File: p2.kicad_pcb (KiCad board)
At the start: 2 copper layers, 66 x 57 mm, 33 parts, among them J1 BARREL_JACK, J2 FLASH_JMP, J3 UART, J4 ALT_POWER, J5 jack-3.5mm-5pin, J6 jack-3.5mm-5pin, J7 jack-3.5mm-5pin, J8 jack-3.5mm-5pin, Q1 IRL540N, Q2 IRL540N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

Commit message: update to pcb-rev1.1
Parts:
- removed the REF** at (31.0, 23.5)
- removed the REF** at (31.0, 73.5)
- removed the REF*** at (47.0, 40.0)
- added REF**: Symbol_CreativeCommons_CopperTop_Type2_Small, Symbols:Symbol_CreativeCommons_CopperTop_Type2_Small, F.Cu at (34.0, 40.5)
- added REF**: Symbol_CC-ShareAlike_CopperTop_Small, Symbols:Symbol_CC-ShareAlike_CopperTop_Small, F.Cu at (45.0, 40.5)
- added REF**: Symbol_CC-Attribution_CopperTop_Small, Symbols:Symbol_CC-Attribution_CopperTop_Small, F.Cu at (39.5, 40.5)
- added REF***: OSHW-Logo2_9.8x8mm_SilkScreen, Symbols:OSHW-Logo2_9.8x8mm_SilkScreen, B.Cu at (58.5, 35.0)
- moved REF** 9.50 mm to (72.0, 36.0)
- moved G*** 1.29 mm to (72.5, 35.0)
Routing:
- net /12V: track 138.4 -> 133.4 mm
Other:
- outline, holes or cut-outs redrawn
- board text added: "+12V"
- board text added: "GND"
- board text added: "Short to flash"
- board text added: "WaterControl v2 r1.1"
- board text added: "designed with"
- board text added: "https://github.com/mqus/watercontrol-pcb.git"
- board text removed: "Flash"
- board text removed: "GND+12V"
- board text removed: "made with"

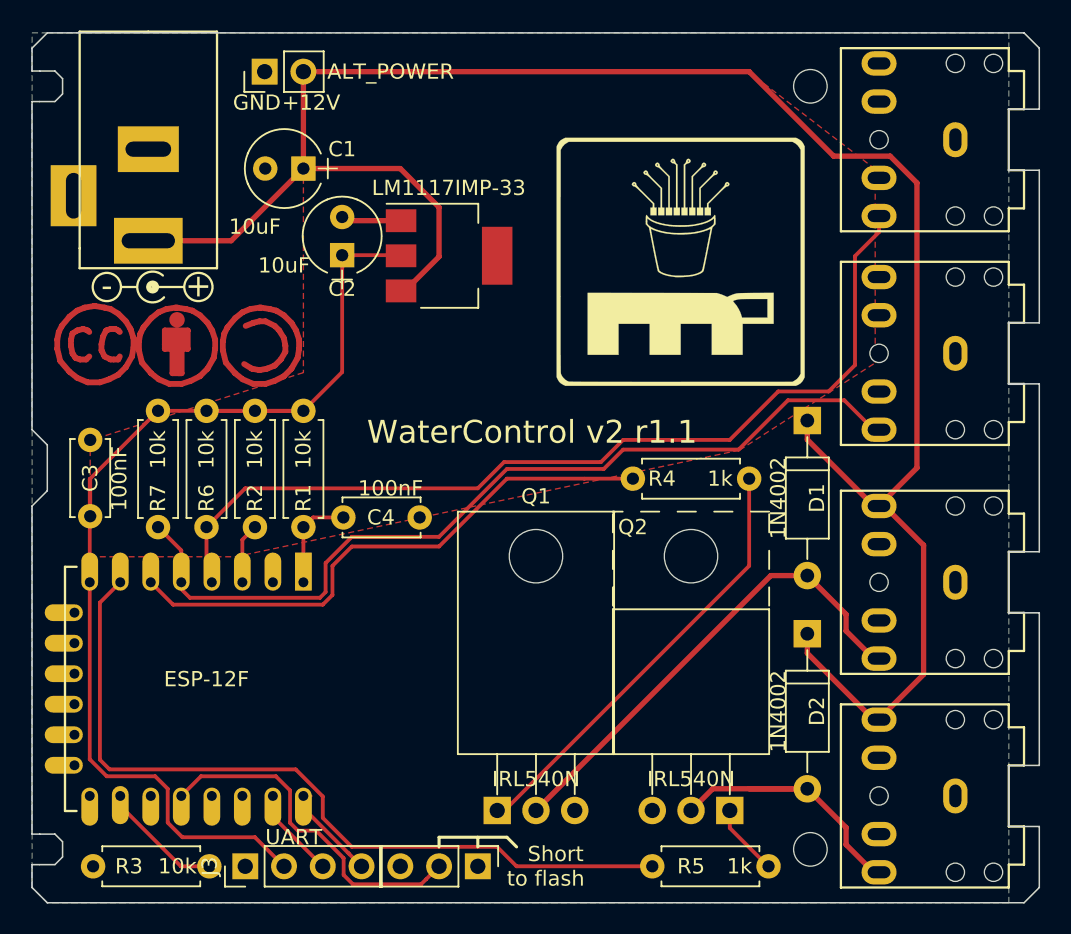
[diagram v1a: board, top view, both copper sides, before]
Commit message: update pcb to rev 1.3 (added copper pours)
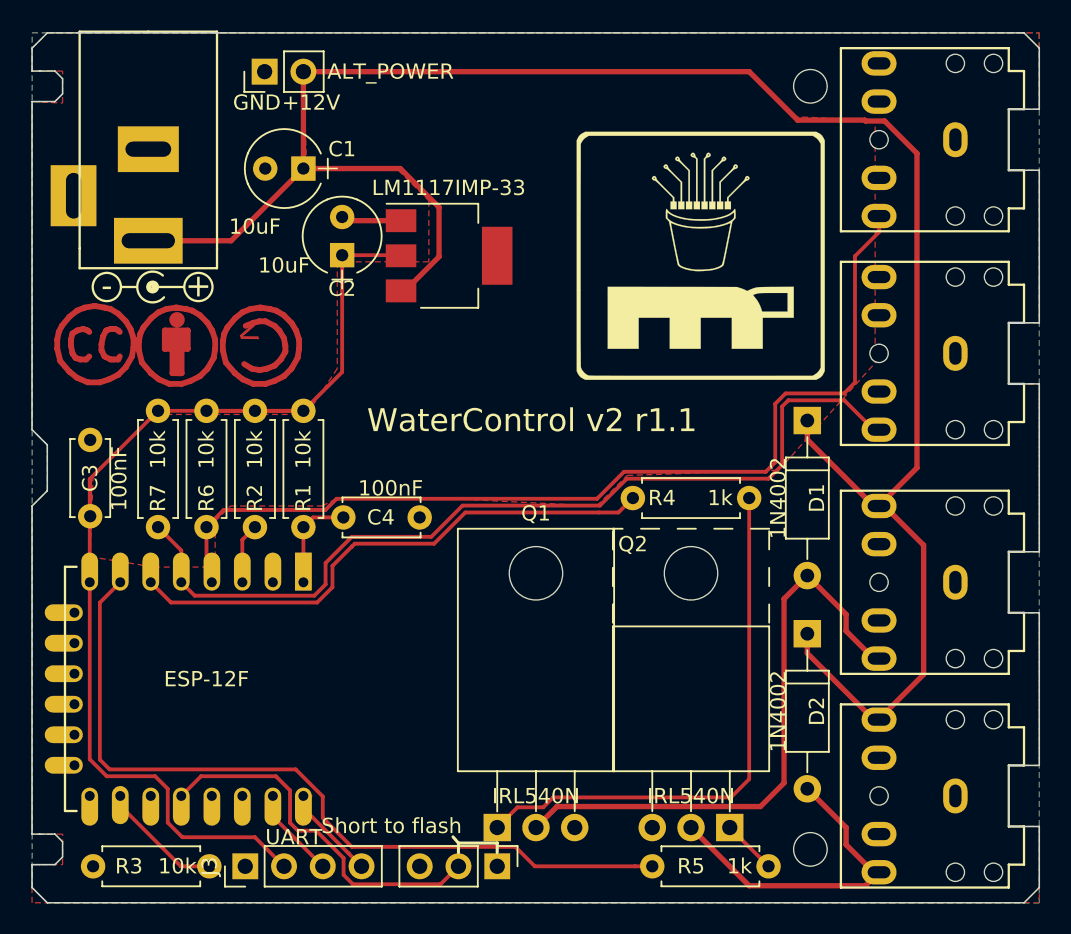
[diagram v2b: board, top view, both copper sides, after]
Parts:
- moved G*** 1.37 mm to (73.8, 34.6)
- moved J2 1.27 mm to (60.5, 74.6)
- moved R4 1.27 mm to (77.0, 50.5)
- moved Q1 1.12 mm to (60.5, 72.1)
- moved Q2 1.12 mm to (75.7, 72.1)
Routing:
- net Net-(D1-Pad2): track 31.7 -> 39.3 mm
- net Net-(Q1-Pad1): track 28.9 -> 36.2 mm
- net /ctl1: track 61.1 -> 64.0 mm
- net /ctl2: track 57.9 -> 59.5 mm
- net /GPIO0: track 22.7 -> 24.0 mm
- net /12V: track 133.4 -> 134.5 mm
- net Net-(Q2-Pad1): track 4.73 -> 3.62 mm
- net /ctl3: track 37.0 -> 36.0 mm
- added copper zone on F.Cu, net (none)
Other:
- board text added: "v"
